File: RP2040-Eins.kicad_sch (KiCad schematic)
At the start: 55 parts, among them J1 CONN_PWR, J10 CONN_USB, J2 CONN_ICSP, J3 CONN_A, J4 CONN_P, J5 CONN_X, J7 CONN_JTAG, J8 CONN_D1, J9 CONN_D2, Q1 AO3401A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

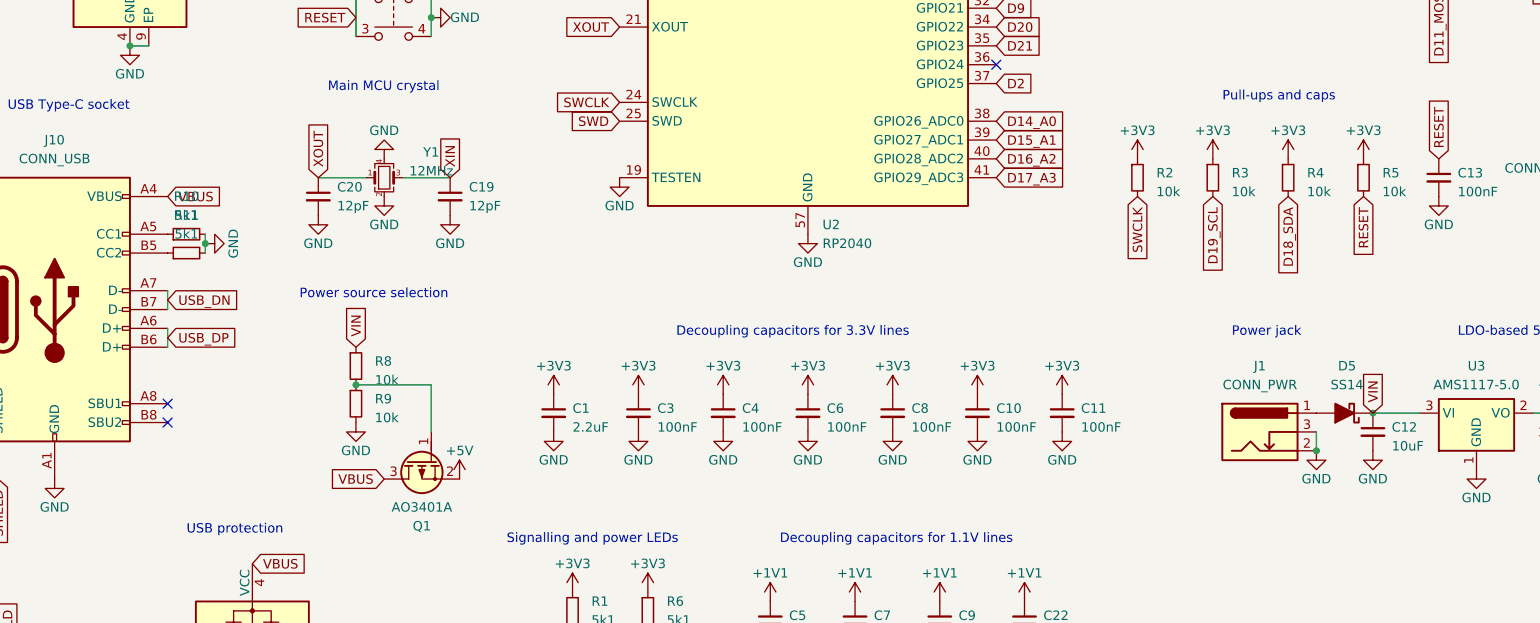
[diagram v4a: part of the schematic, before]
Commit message: Added ferrite beads. Changed power routing.
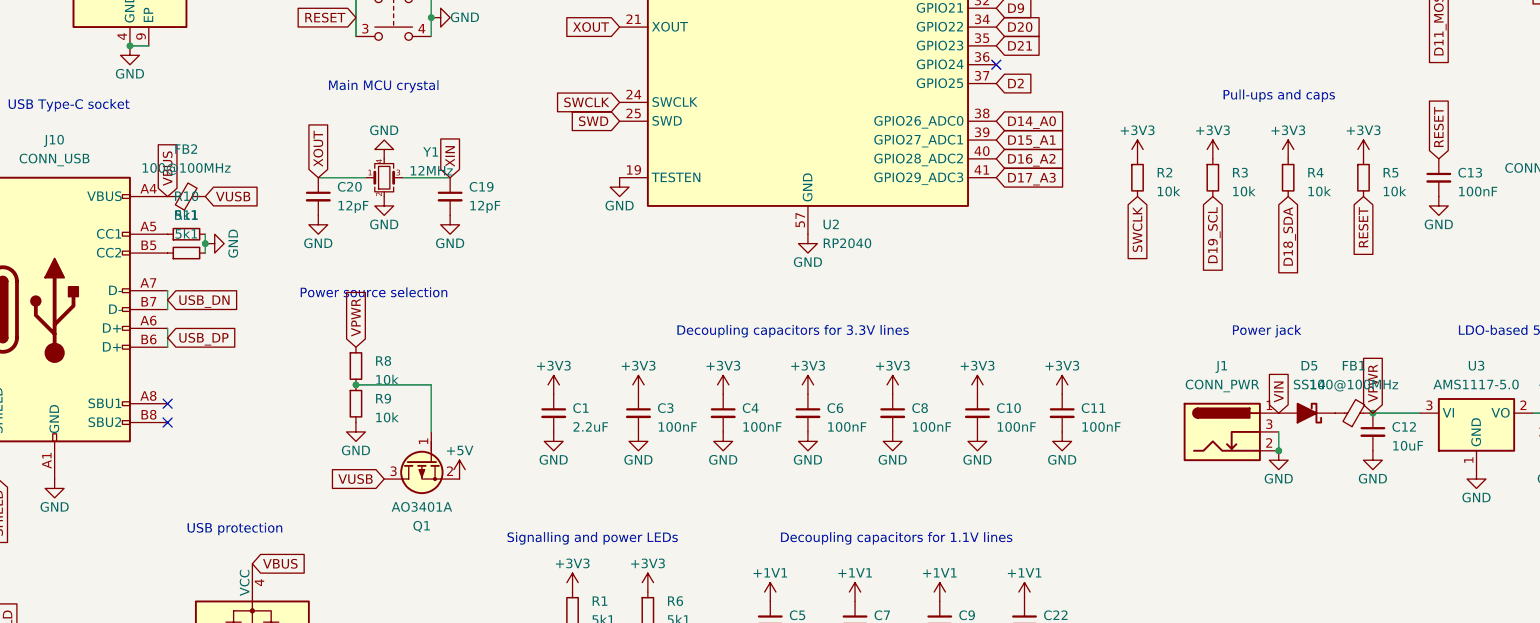
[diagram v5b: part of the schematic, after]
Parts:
- added FB1, FB2: 100@100MHz, Inductor_SMD:L_0805_2012Metric, symbol Device:FerriteBead_Small
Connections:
- net VBUS: now also FB2.1; no longer Q1.3 (D)
- net VIN: now also D5.2 (A), J1.1; no longer C12.1, D5.1 (K), R8.1, U3.3 (VI)
- new net: D5.1 (K), FB1.1
- new net VPWR: C12.1, FB1.2, R8.1, U3.3 (VI)
- new net VUSB: FB2.2, Q1.3 (D)
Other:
- moved on the sheet: D5, J1
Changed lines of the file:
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@@
     (comment 2 "Designed in Germany")
   )
-  (junction (at 209.55 151.13) (diameter 0) (color 0 0 0 0)
-  )
-  (junction (at 217.17 146.05) (diameter 0) (color 0 0 0 0)
+  (junction (at 204.47 151.13) (diameter 0) (color 0 0 0 0)
   )
   (junction (at 148.59 30.48) (diameter 0) (color 0 0 0 0)
@@
   (junction (at 90.17 92.71) (diameter 0) (color 0 0 0 0)
   )
+  (junction (at 217.17 146.05) (diameter 0) (color 0 0 0 0)
+  )
   (junction (at 135.89 30.48) (diameter 0) (color 0 0 0 0)
   )
@@
     (stroke (width 0) (type default))
   )
-  (wire (pts (xy 209.55 148.59) (xy 209.55 151.13))
+  (wire (pts (xy 204.47 148.59) (xy 204.47 151.13))
     (stroke (width 0) (type default))
   )
@@
     )
   )
-  (global_label "VIN" (shape input) (at 80.01 137.16 90) (fields_autoplaced)
+  (global_label "VPWR" (shape input) (at 80.01 137.16 90) (fields_autoplaced)
     (effects (font (size 1.27 1.27)) (justify left))
-    (property "Intersheetrefs" "${INTERSHEET_REFS}" (at 80.01 131.1509 90)
+    (property "Intersheetrefs" "${INTERSHEET_REFS}" (at 80.01 129.0948 90)
       (effects (font (size 1.27 1.27)) (justify left) hide)
     )
@@
     )
   )
+  (global_label "VUSB" (shape input) (at 59.69 116.84 0) (fields_autoplaced)
+    (effects (font (size 1.27 1.27)) (justify left))
+    (property "Intersheetrefs" "${INTERSHEET_REFS}" (at 67.5738 116.84 0)
+      (effects (font (size 1.27 1.27)) (justify left) hide)
+    )
+  )
   (global_label "QSPI_SCLK" (shape input) (at 39.37 78.74 180) (fields_autoplaced)
     (effects (font (size 1.27 1.27)) (justify right))
@@
     )
   )
+  (global_label "VPWR" (shape input) (at 217.17 146.05 90) (fields_autoplaced)
+    (effects (font (size 1.27 1.27)) (justify left))
+    (property "Intersheetrefs" "${INTERSHEET_REFS}" (at 217.17 137.9848 90)
+      (effects (font (size 1.27 1.27)) (justify left) hide)
+    )
+  )
   (global_label "D15_A1" (shape input) (at 203.2 66.04 180) (fields_autoplaced)
     (effects (font (size 1.27 1.27)) (justify right))
@@
     )
   )
-  (global_label "VIN" (shape input) (at 217.17 146.05 90) (fields_autoplaced)
+  (global_label "VIN" (shape input) (at 204.47 146.05 90) (fields_autoplaced)
     (effects (font (size 1.27 1.27)) (justify left))
-    (property "Intersheetrefs" "${INTERSHEET_REFS}" (at 217.17 140.0409 90)
+    (property "Intersheetrefs" "${INTERSHEET_REFS}" (at 204.47 140.0409 90)
       (effects (font (size 1.27 1.27)) (justify left) hide)
     )
@@
     )
   )
-  (global_label "VBUS" (shape input) (at 54.61 116.84 0) (fields_autoplaced)
+  (global_label "VBUS" (shape input) (at 54.61 116.84 90) (fields_autoplaced)
     (effects (font (size 1.27 1.27)) (justify left))
-    (property "Intersheetrefs" "${INTERSHEET_REFS}" (at 62.4938 116.84 0)
+    (property "Intersheetrefs" "${INTERSHEET_REFS}" (at 54.61 108.9562 90)
       (effects (font (size 1.27 1.27)) (justify left) hide)
     )
@@
     )
   )
-  (global_label "VBUS" (shape input) (at 83.82 154.94 180) (fields_autoplaced)
+  (global_label "VUSB" (shape input) (at 83.82 154.94 180) (fields_autoplaced)
     (effects (font (size 1.27 1.27)) (justify right))
     (property "Intersheetrefs" "${INTERSHEET_REFS}" (at 75.9362 154.94 0)
@@
     )
   )
-  (symbol (lib_id "PCM_Diode_Schottky_AKL:SS14") (at 213.36 146.05 0) (unit 1)
+  (symbol (lib_id "PCM_Diode_Schottky_AKL:SS14") (at 208.28 146.05 0) (unit 1)
     (in_bom yes) (on_board yes) (dnp no) (fields_autoplaced)
-    (property "Reference" "D5" (at 213.6775 139.7 0)
+    (property "Reference" "D5" (at 208.5975 139.7 0)
       (effects (font (size 1.27 1.27)))
     )
-    (property "Value" "SS14" (at 213.6775 142.24 0)
+    (property "Value" "SS14" (at 208.5975 142.24 0)
       (effects (font (size 1.27 1.27)))
     )
-    (property "Footprint" "PCM_4ms_Diode:D_DO-214AC_SMA" (at 213.36 146.05 0)
+    (property "Footprint" "PCM_4ms_Diode:D_DO-214AC_SMA" (at 208.28 146.05 0)
       (effects (font (size 1.27 1.27)) hide)
     )
-    (property "Datasheet" "https://www.tme.eu/Document/39e1c2d2c354f63d74e9a2edb2156b4b/SS14-E3_61T.pdf" (at 213.36 146.05 0)
+    (property "Datasheet" "https://www.tme.eu/Document/39e1c2d2c354f63d74e9a2edb2156b4b/SS14-E3_61T.pdf" (at 208.28 146.05 0)
       (effects (font (size 1.27 1.27)) hide)
     )
@@
     )
   )
-  (symbol (lib_id "power:GND") (at 209.55 151.13 0) (unit 1)
+  (symbol (lib_id "power:GND") (at 204.47 151.13 0) (unit 1)
     (in_bom yes) (on_board yes) (dnp no)
-    (property "Reference" "#PWR058" (at 209.55 157.48 0)
+    (property "Reference" "#PWR058" (at 204.47 157.48 0)
       (effects (font (size 1.27 1.27)) hide)
     )
-    (property "Value" "GND" (at 209.55 154.94 0)
+    (property "Value" "GND" (at 204.47 154.94 0)
       (effects (font (size 1.27 1.27)))
     )
-    (property "Footprint" "" (at 209.55 151.13 0)
+    (property "Footprint" "" (at 204.47 151.13 0)
       (effects (font (size 1.27 1.27)) hide)
     )
-    (property "Datasheet" "" (at 209.55 151.13 0)
+    (property "Datasheet" "" (at 204.47 151.13 0)
       (effects (font (size 1.27 1.27)) hide)
     )
@@
     )
   )
+  (symbol (lib_id "Device:FerriteBead_Small") (at 214.63 146.05 90) (unit 1)
+    (in_bom yes) (on_board yes) (dnp no) (fields_autoplaced)
+    (property "Reference" "FB1" (at 214.5919 139.7 90)
+      (effects (font (size 1.27 1.27)))
+    )
+    (property "Value" "100@100MHz" (at 214.5919 142.24 90)
+      (effects (font (size 1.27 1.27)))
+    )
+    (property "Footprint" "Inductor_SMD:L_0805_2012Metric" (at 214.63 147.828 90)
+      (effects (font (size 1.27 1.27)) hide)
+    )
+    (property "Datasheet" "~" (at 214.63 146.05 0)
+      (effects (font (size 1.27 1.27)) hide)
+    )
+    (pin "1")
+    (pin "2")
+    (instances
+      (project "RP2040-Eins"
+        (path "/9a38a81c-7302-494f-9784-2ab4342a0a1d"
+          (reference "FB1") (unit 1)
+        )
+      )
+    )
+  )
   (symbol (lib_id "power:GND") (at 223.52 87.63 270) (unit 1)
     (in_bom yes) (on_board yes) (dnp no)
@@
     )
   )
+  (symbol (lib_id "Device:FerriteBead_Small") (at 57.15 116.84 90) (unit 1)
+    (in_bom yes) (on_board yes) (dnp no) (fields_autoplaced)
+    (property "Reference" "FB2" (at 57.1119 110.49 90)
+      (effects (font (size 1.27 1.27)))
+    )
+    (property "Value" "100@100MHz" (at 57.1119 113.03 90)
+      (effects (font (size 1.27 1.27)))
+    )
+    (property "Footprint" "Inductor_SMD:L_0805_2012Metric" (at 57.15 118.618 90)
+      (effects (font (size 1.27 1.27)) hide)
+    )
+    (property "Datasheet" "~" (at 57.15 116.84 0)
+      (effects (font (size 1.27 1.27)) hide)
+    )
+    (pin "1")
+    (pin "2")
+    (instances
+      (project "RP2040-Eins"
+        (path "/9a38a81c-7302-494f-9784-2ab4342a0a1d"
+          (reference "FB2") (unit 1)
+        )
+      )
+    )
+  )
   (symbol (lib_id "Device:C_Small") (at 152.4 146.05 0) (unit 1)
     (in_bom yes) (on_board yes) (dnp no) (fields_autoplaced)
@@
     )
   )
-  (symbol (lib_id "Connector:Barrel_Jack_Switch") (at 201.93 148.59 0) (unit 1)
+  (symbol (lib_id "Connector:Barrel_Jack_Switch") (at 196.85 148.59 0) (unit 1)
     (in_bom yes) (on_board yes) (dnp no) (fields_autoplaced)
-    (property "Reference" "J1" (at 201.93 139.7 0)
+    (property "Reference" "J1" (at 196.85 139.7 0)
       (effects (font (size 1.27 1.27)))
     )
-    (property "Value" "CONN_PWR" (at 201.93 142.24 0)
+    (property "Value" "CONN_PWR" (at 196.85 142.24 0)
       (effects (font (size 1.27 1.27)))
     )
-    (property "Footprint" "Connector_BarrelJack:BarrelJack_Horizontal" (at 203.2 149.606 0)
+    (property "Footprint" "Connector_BarrelJack:BarrelJack_Horizontal" (at 198.12 149.606 0)
       (effects (font (size 1.27 1.27)) hide)
     )
-    (property "Datasheet" "~" (at 203.2 149.606 0)
+    (property "Datasheet" "~" (at 198.12 149.606 0)
       (effects (font (size 1.27 1.27)) hide)
     )

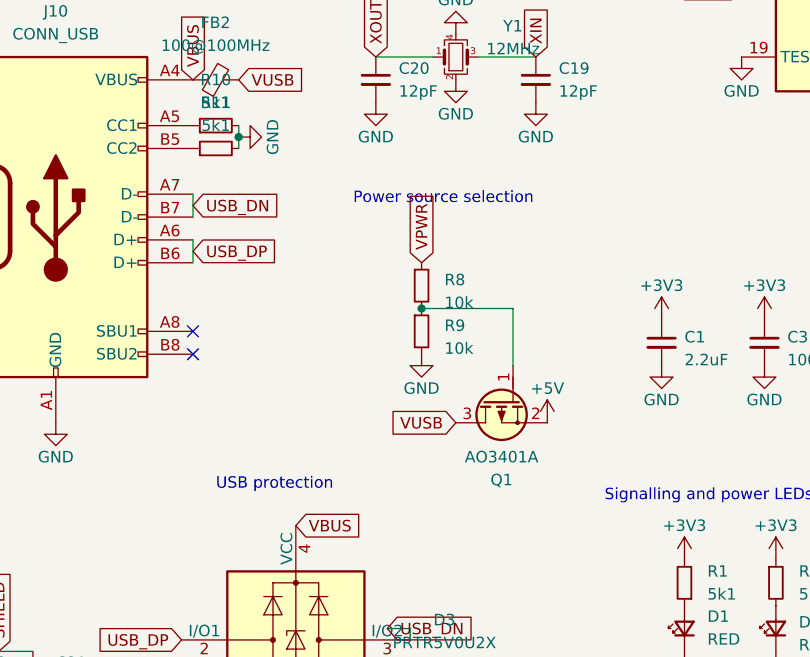
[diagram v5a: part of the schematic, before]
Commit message: Added few traces
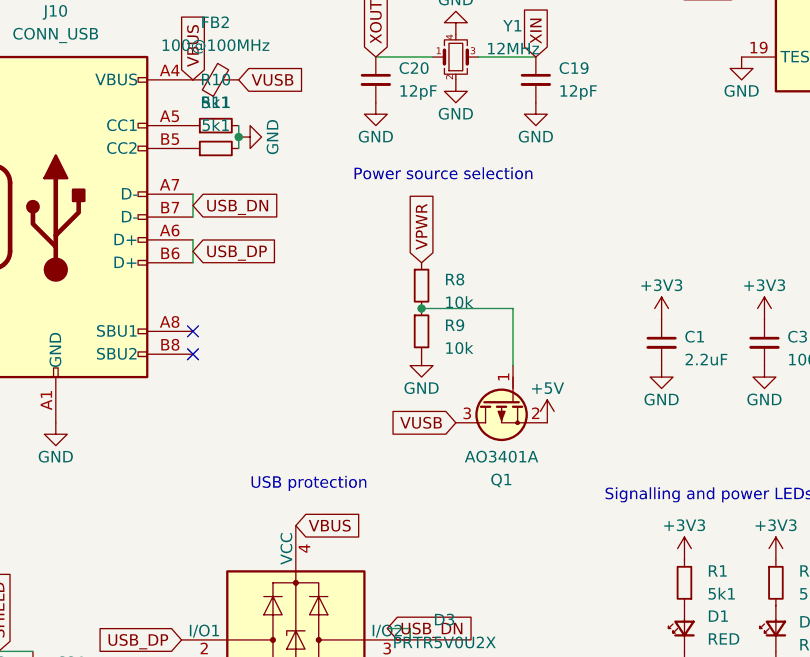
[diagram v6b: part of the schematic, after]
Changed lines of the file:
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@@
     (stroke (width 0) (type default))
   )
-  (text "USB protection" (at 57.15 162.56 0)
+  (text "USB protection" (at 60.96 162.56 0)
     (effects (font (size 1.27 1.27)) (justify left bottom))
   )
@@
     (effects (font (size 1.27 1.27)) (justify left bottom))
   )
-  (text "Power source selection" (at 72.39 130.81 0)
+  (text "Power source selection" (at 72.39 128.27 0)
     (effects (font (size 1.27 1.27)) (justify left bottom))
   )

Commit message: Moved stuff around
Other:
- moved on the sheet: C1, C10, C11, C12, C13, C14, C15, C19, C20, C21, C22, C3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
